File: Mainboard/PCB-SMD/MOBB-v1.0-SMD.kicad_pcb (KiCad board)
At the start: 2 copper layers, 85.6 x 49.7 mm, 68 parts, among them P1 AUX 1-3, P14 EXTRA Pins, P2 VUSB, P3 +3.3V, P4 Pit Limiter, P5 Rotary Encoders, P6 BTN 1-32, P7 LED, Q1 NPN, Q2 NPN, Q3 NPN, Q4 NPN, U1 74HC4051, U2 74HC4051, U3 74HC4051, U4 74HC4051, U5 Teensy3.2

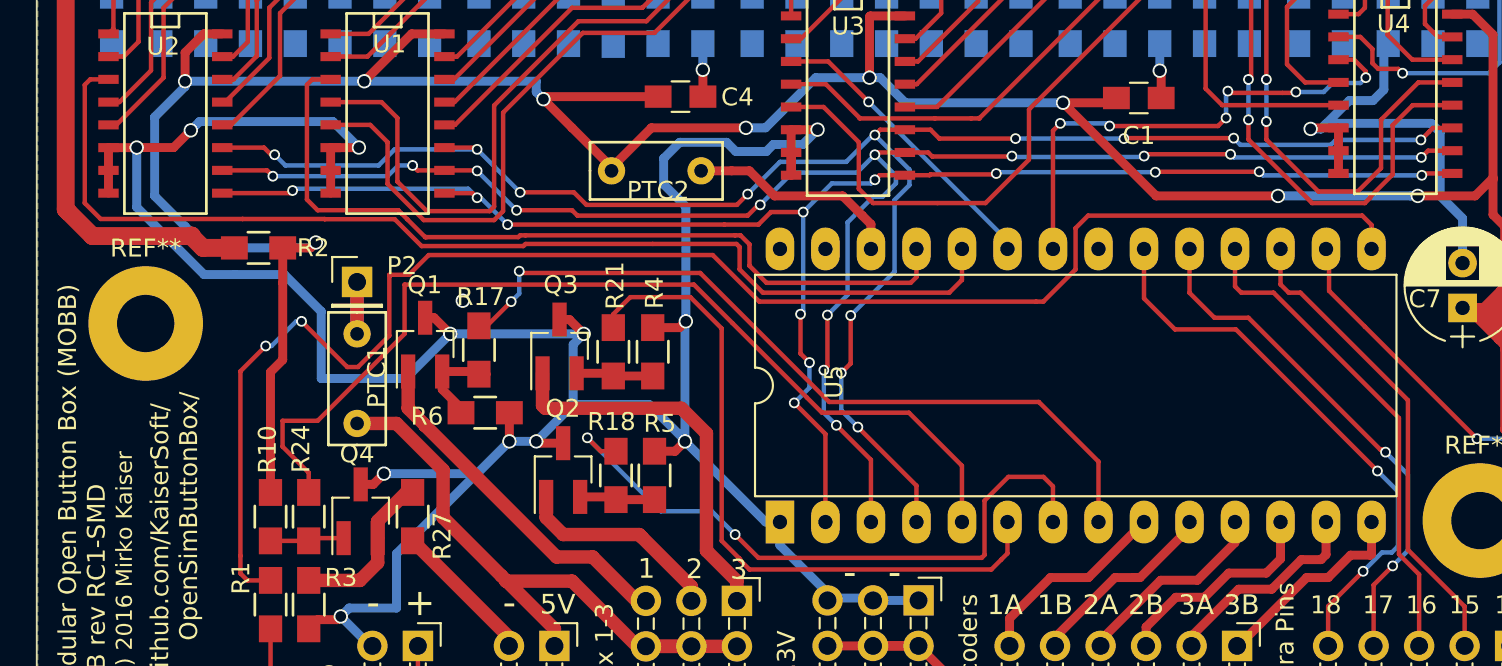
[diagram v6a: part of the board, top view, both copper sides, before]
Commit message: * SMD PCB tweaked
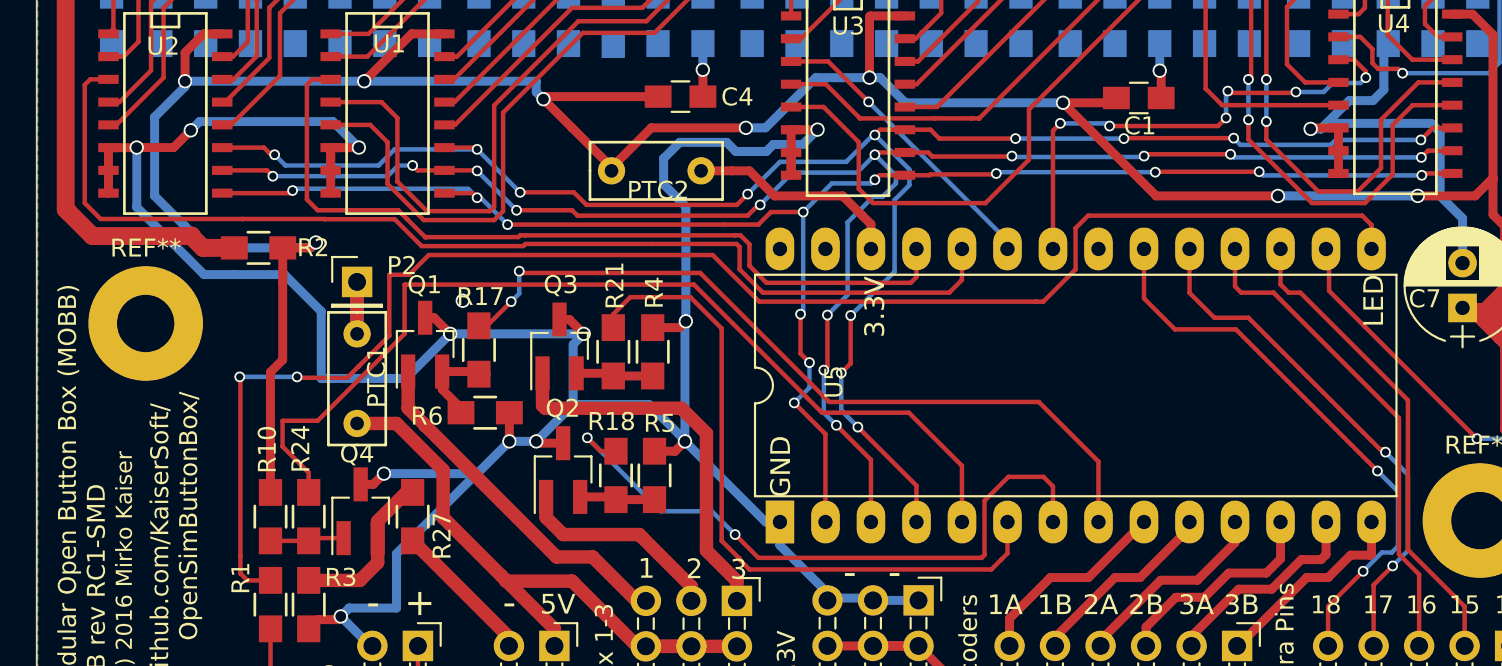
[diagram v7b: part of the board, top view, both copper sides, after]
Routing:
- net GND: track 191.8 -> 195.6 mm
- net Net-(R1-Pad1): track 89.1 -> 87.0 mm
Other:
- board text added: "3.3V"
- board text added: "GND"
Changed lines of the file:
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@@
   (general
     (links 220)
-    (no_connects 35)
-    (area 175.269999 94.979999 260.970001 144.820001)
+    (no_connects 32)
+    (area 173.275 88.574999 267.312858 151.241001)
     (thickness 1.6)
-    (drawings 94)
-    (tracks 1029)
+    (drawings 97)
+    (tracks 1033)
     (zones 0)
     (modules 68)
@@
     (tags "capacitor 0805")
     (attr smd)
-    (fp_text reference C1 (at 0 -2.1 180) (layer F.SilkS)
+    (fp_text reference C1 (at -0.0704 -1.5656 180) (layer F.SilkS)
       (effects (font (size 1 1) (thickness 0.15)))
     )
@@
       (effects (font (size 1 1) (thickness 0.15)))
     )
-    (fp_text value NPN (at 0 2.5 90) (layer F.Fab)
+    (fp_text value NPN (at -0.05 0.35 90) (layer F.Fab)
       (effects (font (size 1 1) (thickness 0.15)))
     )
@@
       (effects (font (size 1 1) (thickness 0.15)))
     )
-    (fp_text value NPN (at 0 2.5 90) (layer F.Fab)
+    (fp_text value NPN (at -0.1 0.05 90) (layer F.Fab)
       (effects (font (size 1 1) (thickness 0.15)))
     )
@@
       (effects (font (size 1 1) (thickness 0.15)))
     )
-    (fp_text value NPN (at 0 2.5 90) (layer F.Fab)
+    (fp_text value NPN (at -0.15 0.2 90) (layer F.Fab)
       (effects (font (size 1 1) (thickness 0.15)))
     )
@@
       (effects (font (size 1 1) (thickness 0.15)))
     )
-    (fp_text value NPN (at 0 2.5 90) (layer F.Fab)
+    (fp_text value NPN (at -0.35 0.05 90) (layer F.Fab)
       (effects (font (size 1 1) (thickness 0.15)))
     )
@@
       (effects (font (size 1 1) (thickness 0.15)))
     )
-    (fp_text value 10K (at 0 2.1 270) (layer F.Fab)
+    (fp_text value 10K (at 0.24 -0.08 270) (layer F.Fab)
       (effects (font (size 1 1) (thickness 0.15)))
     )
@@
       (effects (font (size 1 1) (thickness 0.15)))
     )
-    (fp_text value 10K (at 0 2.1 90) (layer F.Fab)
+    (fp_text value 10K (at 0.01 0.15 90) (layer F.Fab)
       (effects (font (size 1 1) (thickness 0.15)))
     )
@@
       (effects (font (size 1 1) (thickness 0.15)))
     )
-    (fp_text value 100K (at 0 2.1 270) (layer F.Fab)
+    (fp_text value 100K (at 0.0976 -0.0336 270) (layer F.Fab)
       (effects (font (size 1 1) (thickness 0.15)))
     )
@@
       (effects (font (size 1 1) (thickness 0.15)))
     )
-    (fp_text value 1K (at 0 2.1 90) (layer F.Fab)
+    (fp_text value 1K (at 0.1 0.05 90) (layer F.Fab)
       (effects (font (size 1 1) (thickness 0.15)))
     )
@@
       (effects (font (size 1 1) (thickness 0.15)))
     )
-    (fp_text value 1K (at 0 2.1 270) (layer F.Fab)
+    (fp_text value 1K (at -0.15 0 270) (layer F.Fab)
       (effects (font (size 1 1) (thickness 0.15)))
     )
@@
       (effects (font (size 1 1) (thickness 0.15)))
     )
-    (fp_text value 74HC4051 (at 0 1.27 270) (layer F.Fab)
+    (fp_text value 74HC4051 (at 1.2 0.1 270) (layer F.Fab)
       (effects (font (size 1 1) (thickness 0.15)))
     )
@@
       (effects (font (size 1 1) (thickness 0.15)))
     )
-    (fp_text value 74HC4051 (at 0 1.27 270) (layer F.Fab)
+    (fp_text value 74HC4051 (at 0.7 0.1 270) (layer F.Fab)
       (effects (font (size 1 1) (thickness 0.15)))
     )
@@
       (effects (font (size 1 1) (thickness 0.15)))
     )
-    (fp_text value 74HC4051 (at 0 1.27 270) (layer F.Fab)
+    (fp_text value 74HC4051 (at 1.25 0.35 270) (layer F.Fab)
       (effects (font (size 1 1) (thickness 0.15)))
     )
@@
       (effects (font (size 1 1) (thickness 0.15)))
     )
-    (fp_text value 74HC4051 (at 0 1.27 270) (layer F.Fab)
+    (fp_text value 74HC4051 (at 1.45 0.1 270) (layer F.Fab)
       (effects (font (size 1 1) (thickness 0.15)))
     )
@@
       (effects (font (size 1 1) (thickness 0.15)))
     )
-    (fp_text value MountingHole_3.2mm_M3_Pad (at 0 4.2) (layer F.Fab)
+    (fp_text value MountingHole_3.2mm_M3_Pad (at 5.98 -0.07 90) (layer F.Fab)
       (effects (font (size 1 1) (thickness 0.15)))
     )
@@
     )
   )
+  (gr_text 3.3V (at 222.1 121.8 90) (layer F.SilkS)
+    (effects (font (size 1.1 1.1) (thickness 0.2)))
+  )
+  (gr_text LED (at 249.95 121.45 90) (layer F.SilkS)
+    (effects (font (size 1.1 1.1) (thickness 0.2)))
+  )
+  (gr_text GND (at 216.85 130.7 90) (layer F.SilkS)
+    (effects (font (size 1.1 1.1) (thickness 0.2)))
+  )
   (gr_text - (at 194.1 138.3) (layer F.SilkS)
     (effects (font (size 1.5 1.5) (thickness 0.3)))
@@
     (effects (font (size 0.9 0.9) (thickness 0.15)))
   )
-  (gr_text "(c) 2016 Mirko Kaiser" (at 235.3564 128.1938) (layer B.SilkS)
+  (gr_text "(c) 2016 Mirko Kaiser" (at 241.35 128.25) (layer B.SilkS)
     (effects (font (size 1.2 1.2) (thickness 0.25)) (justify mirror))
   )
@@
     (effects (font (size 1.1 1.1) (thickness 0.2)))
   )
-  (gr_text github.com/KaiserSoft/OpenSimButtonBox (at 228.6 125.9332) (layer B.SilkS)
+  (gr_text github.com/KaiserSoft/OpenSimButtonBox (at 234.6 125.95) (layer B.SilkS)
     (effects (font (size 1.05 1.05) (thickness 0.25)) (justify mirror))
   )
-  (gr_text "Modular Open Button Box (MOBB)" (at 245.5418 123.7742) (layer B.SilkS)
+  (gr_text "Modular Open Button Box (MOBB)" (at 251.55 123.75) (layer B.SilkS)
     (effects (font (size 1.5 1.5) (thickness 0.3)) (justify left mirror))
   )
@@
   (segment (start 193.6 109.2) (end 196.245 106.555) (width 0.5) (layer F.Cu) (net 5))
   (segment (start 196.245 106.555) (end 198.075 106.555) (width 0.5) (layer F.Cu) (net 5))
+  (segment (start 247.975 113.075) (end 247.975 111.805) (width 0.5) (layer F.Cu) (net 6) (status C00000))
+  (segment (start 191.725 114.175) (end 191.725 112.905) (width 0.5) (layer F.Cu) (net 6) (status C00000))
+  (segment (start 179.325 115.445) (end 179.325 114.175) (width 0.5) (layer F.Cu) (net 6) (status C00000))
   (segment (start 191.2 125.79) (end 191.2 122.05) (width 0.5) (layer B.Cu) (net 6))
   (segment (start 189.14 119.99) (end 186.39 119.99) (width 0.5) (layer B.Cu) (net 6))
@@
   (segment (start 192.45 134.7) (end 190.65 134.7) (width 0.25) (layer F.Cu) (net 62))
   (segment (start 190.65 134.7) (end 190.5 134.85) (width 0.25) (layer F.Cu) (net 62))
-  (segment (start 193.2 123.3) (end 193.2 120.4) (width 0.75) (layer B.Cu) (net 63) (status C00000))
-  (segment (start 193.2 120.4) (end 193.2 123.3) (width 0.75) (layer F.Cu) (net 63) (status C00000))
+  (segment (start 193.2 123.3) (end 193.2 120.4) (width 0.75) (layer B.Cu) (net 63))
+  (segment (start 193.2 120.4) (end 193.2 123.3) (width 0.75) (layer F.Cu) (net 63))
   (segment (start 183.97 117.812502) (end 183.97 117.87) (width 1) (layer F.Cu) (net 64))
   (segment (start 183.97 117.84) (end 183.97 117.812502) (width 1) (layer F.Cu) (net 64))
@@
   (segment (start 222 118.44) (end 221.88 118.56) (width 0.5) (layer F.Cu) (net 65))
   (segment (start 212.4 114.2) (end 212.5 114.2) (width 0.5) (layer F.Cu) (net 65))
-  (segment (start 190.1 122.6) (end 192.65 125.15) (width 0.25) (layer F.Cu) (net 66))
+  (segment (start 193.275 125.125) (end 192.65 125.75) (width 0.25) (layer F.Cu) (net 66))
+  (segment (start 189.9 125.75) (end 189.85 125.7) (width 0.25) (layer F.Cu) (net 66))
+  (segment (start 192.65 125.75) (end 189.9 125.75) (width 0.25) (layer F.Cu) (net 66))
+  (via (at 186.65 125.7) (size 0.6) (drill 0.4) (layers F.Cu B.Cu) (net 66))
+  (via (at 189.85 125.7) (size 0.6) (drill 0.4) (layers F.Cu B.Cu) (net 66))
+  (segment (start 189.85 125.7) (end 186.65 125.7) (width 0.25) (layer B.Cu) (net 66))
+  (segment (start 186.65 125.7) (end 186.69 125.7) (width 0.25) (layer F.Cu) (net 66))
+  (segment (start 186.69 125.7) (end 186.65 125.7) (width 0.25) (layer F.Cu) (net 66))
+  (segment (start 186.65 125.7) (end 186.69 125.7) (width 0.25) (layer F.Cu) (net 66))
   (segment (start 195.05 120.05) (end 195.05 120) (width 0.25) (layer F.Cu) (net 66))
   (segment (start 195 120) (end 195.05 120.05) (width 0.25) (layer F.Cu) (net 66))
   (segment (start 195 123.4) (end 195 120) (width 0.25) (layer F.Cu) (net 66))
-  (segment (start 193.25 125.15) (end 195 123.4) (width 0.25) (layer F.Cu) (net 66))
-  (segment (start 192.65 125.15) (end 193.25 125.15) (width 0.25) (layer F.Cu) (net 66))
+  (segment (start 193.275 125.125) (end 195 123.4) (width 0.25) (layer F.Cu) (net 66))
   (segment (start 188.37 137.06) (end 187.08 137.06) (width 0.25) (layer F.Cu) (net 66))
-  (segment (start 188.1 123.975) (end 188.425 123.975) (width 0.25) (layer B.Cu) (net 66))
-  (segment (start 186.69 135.69) (end 186.69 125.385) (width 0.25) (layer F.Cu) (net 66))
-  (via (at 188.1 123.975) (size 0.6) (drill 0.4) (layers F.Cu B.Cu) (net 66))
-  (segment (start 186.69 125.385) (end 188.1 123.975) (width 0.25) (layer F.Cu) (net 66))
-  (via (at 190.1 122.6) (size 0.6) (drill 0.4) (layers F.Cu B.Cu) (net 66))
-  (segment (start 189.8 122.6) (end 190.1 122.6) (width 0.25) (layer B.Cu) (net 66))
-  (segment (start 188.425 123.975) (end 189.8 122.6) (width 0.25) (layer B.Cu) (net 66))
+  (segment (start 186.69 135.69) (end 186.69 125.7) (width 0.25) (layer F.Cu) (net 66))
   (segment (start 195.05 120) (end 195.8 120) (width 0.25) (layer F.Cu) (net 66))
   (segment (start 231.1 121.5) (end 231.5 121.5) (width 0.25) (layer F.Cu) (net 66))
